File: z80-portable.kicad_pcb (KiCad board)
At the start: 2 copper layers, 131.3 x 89.9 mm, 46 parts, among them J1 Conn_01x40, J2 Barrel_Jack_MountingPin, J3 Conn_01x03, J4 Conn_01x06, J5 Conn_01x14, SW1 SW_Push, U1 74HC157, U10 DS1233-5+, U11 L7805, U2 74HC137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

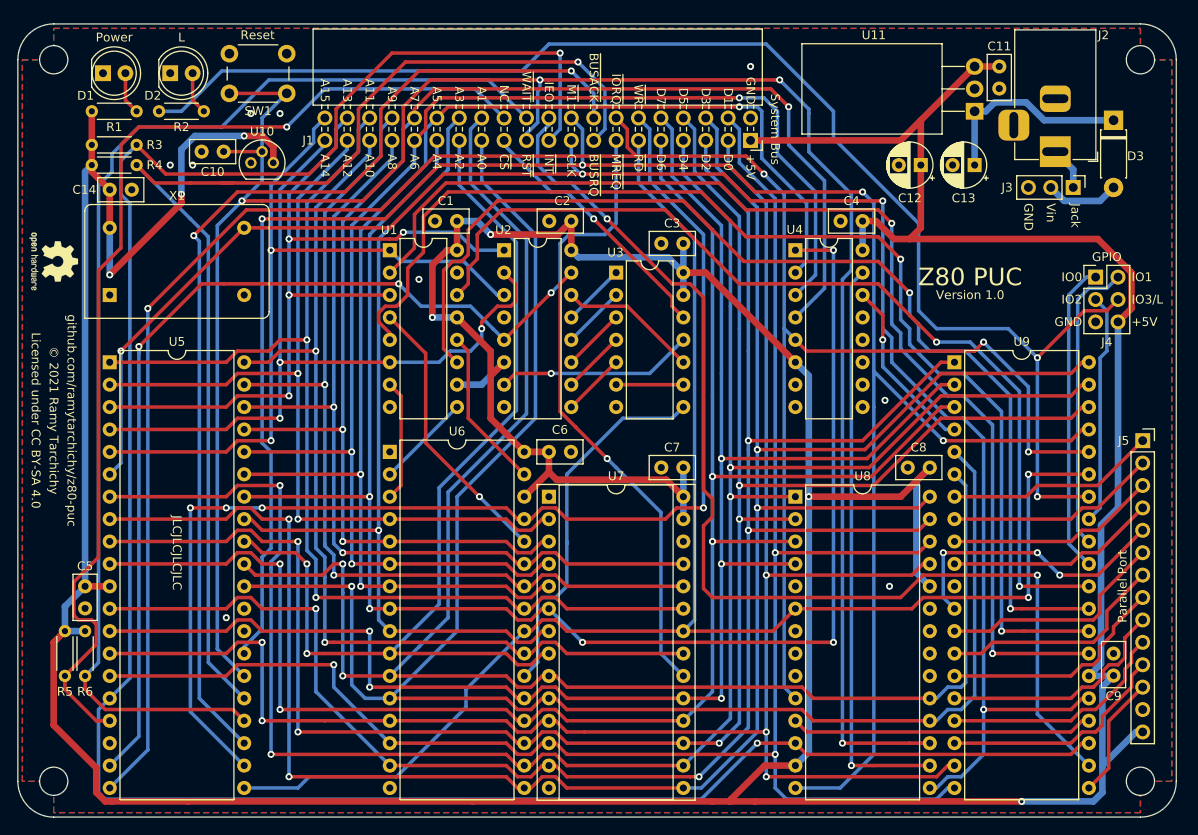
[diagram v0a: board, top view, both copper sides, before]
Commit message: Fixed a few minor mistakes, no need to reorder PCB
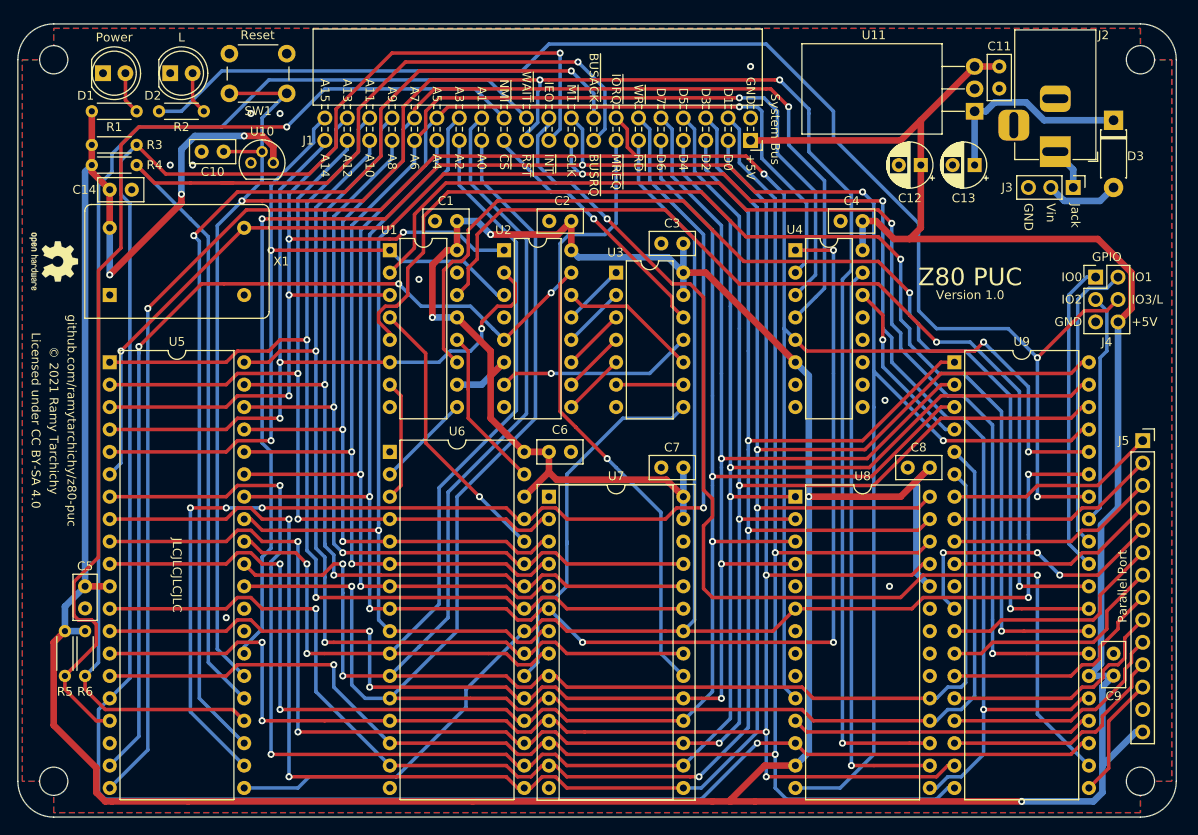
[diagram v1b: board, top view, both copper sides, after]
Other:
- board text added: "~NMI"
- board text removed: "NC"
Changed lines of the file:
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@@
   )
   (setup
-    (last_trace_width 0.4)
+    (last_trace_width 0.25)
     (user_trace_width 0.4)
     (user_trace_width 0.75)
@@
     (descr "Oscillator, DIP14, http://cdn-reichelt.de/documents/datenblatt/B400/OSZI.pdf")
     (tags oscillator)
-    (fp_text reference X1 (at 7.62 -11.26) (layer F.SilkS)
-      (effects (font (size 1 1) (thickness 0.15)))
+    (fp_text reference X1 (at 18.542 -3.81) (layer F.SilkS)
+      (effects (font (size 1 1) (thickness 0.15)) (justify left))
     )
     (fp_text value 10MHz (at 7.62 3.74) (layer F.Fab)
@@
     (arrow2b (pts (xy 63.754 53.848) (xy 64.340421 54.974504)))
   )
-  (gr_text JLCJLCJLCJLC (at 95.504 109.728 270) (layer F.SilkS)
+  (gr_text JLCJLCJLCJLC (at 95.504 112.268 270) (layer F.SilkS)
     (effects (font (size 1 1) (thickness 0.15)))
   )
@@
     (effects (font (size 1 1) (thickness 0.15)) (justify right))
   )
-  (gr_text NC (at 132.588 58.674 -90) (layer F.SilkS)
+  (gr_text ~NMI (at 132.588 58.674 -90) (layer F.SilkS)
     (effects (font (size 1 1) (thickness 0.15)) (justify right))
   )
@@
   (segment (start 200.475999 123.120001) (end 200.475999 123.882001) (width 0.4) (layer F.Cu) (net 60))
   (segment (start 198.12 124.968) (end 199.39 124.968) (width 0.4) (layer F.Cu) (net 60))
-  (segment (start 183.642 123.698) (end 196.85 123.698) (width 0.4) (layer F.Cu) (net 61))
-  (segment (start 196.85 123.698) (end 198.12 122.428) (width 0.4) (layer F.Cu) (net 61))
-  (segment (start 198.12 122.428) (end 199.39 122.428) (width 0.4) (layer F.Cu) (net 61))
-  (segment (start 204.978 114.808) (end 201.676 118.11) (width 0.4) (layer F.Cu) (net 61))
+  (segment (start 202.184 117.602) (end 204.978 114.808) (width 0.4) (layer F.Cu) (net 61))
+  (segment (start 202.184 118.364) (end 202.184 117.602) (width 0.4) (layer F.Cu) (net 61))
+  (segment (start 200.152 120.396) (end 202.184 118.364) (width 0.4) (layer F.Cu) (net 61))
   (segment (start 199.39 122.428) (end 200.152 121.666) (width 0.4) (layer F.Cu) (net 61))
+  (segment (start 198.12 122.428) (end 199.39 122.428) (width 0.4) (layer F.Cu) (net 61))
+  (segment (start 196.85 123.698) (end 198.12 122.428) (width 0.4) (layer F.Cu) (net 61))
   (segment (start 200.152 121.666) (end 200.152 120.396) (width 0.4) (layer F.Cu) (net 61))
-  (segment (start 200.152 120.396) (end 201.676 118.872) (width 0.4) (layer F.Cu) (net 61))
-  (segment (start 201.676 118.872) (end 201.676 118.11) (width 0.4) (layer F.Cu) (net 61))
+  (segment (start 183.642 123.698) (end 196.85 123.698) (width 0.4) (layer F.Cu) (net 61))
   (segment (start 183.642 121.158) (end 186.69 121.158) (width 0.4) (layer F.Cu) (net 62))
   (segment (start 186.69 121.158) (end 187.96 119.888) (width 0.4) (layer F.Cu) (net 62))
